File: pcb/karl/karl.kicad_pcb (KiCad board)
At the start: 2 copper layers, 72.4 x 57.1 mm, 30 parts, among them J1 Raspberry_Pi, J2 Power, J3 Battery, J4 LIDAR_Power, J5 Motor_Power, Q1 MMBT3904, Q2 MMBT3904, U1 MCP3421A0T-ECH

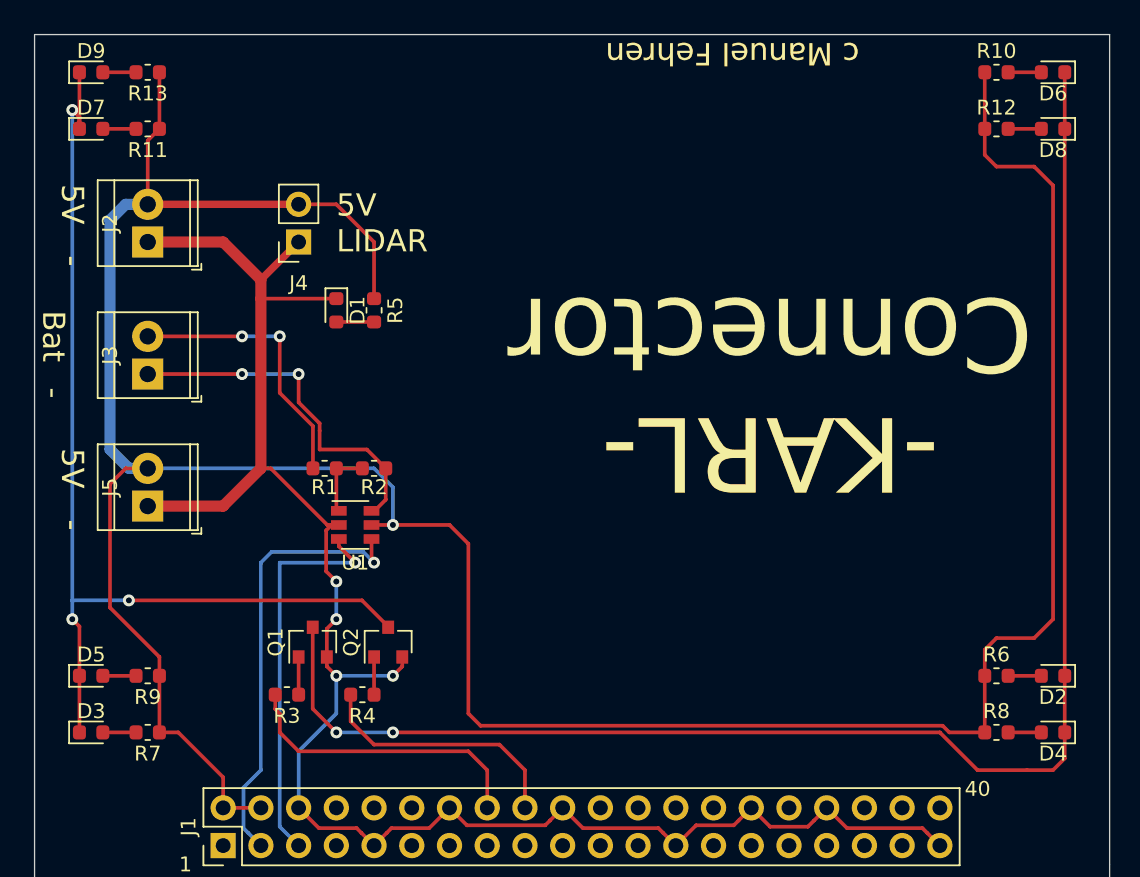
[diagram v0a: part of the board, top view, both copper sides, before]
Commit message: changes screw terminal
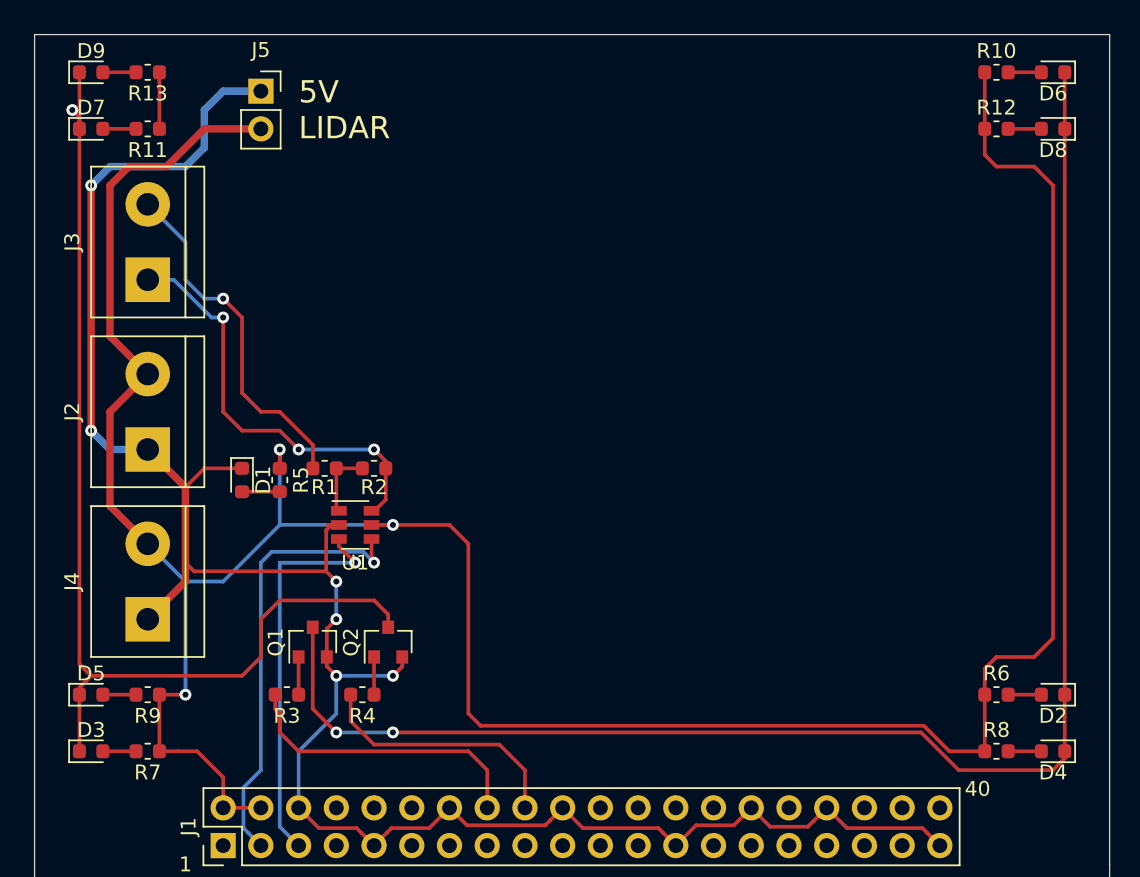
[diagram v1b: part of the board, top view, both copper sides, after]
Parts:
- J2, J3: footprint TerminalBlock_TE-Connectivity:TerminalBlock_TE_282834-2_1x02_P2.54mm_Horizontal -> TerminalBlock:TerminalBlock_bornier-2_P5.08mm
- J4: value LIDAR_Power -> Motor Power; footprint Connector_PinSocket_2.54mm:PinSocket_1x02_P2.54mm_Vertical -> TerminalBlock:TerminalBlock_bornier-2_P5.08mm
- J5: value Motor_Power -> LIDAR_Power; footprint TerminalBlock_TE-Connectivity:TerminalBlock_TE_282834-2_1x02_P2.54mm_Horizontal -> Connector_PinSocket_2.54mm:PinSocket_1x02_P2.54mm_Vertical
- moved J5 29.0 mm to (41.9, 24.1), turned to 0 degrees
- moved J4 27.4 mm to (34.3, 59.7), turned to 90 degrees
- moved J2 14.0 mm to (34.3, 48.3)
- moved D1 13.1 mm to (40.6, 50.3)
- moved R5 13.1 mm to (43.2, 50.3)
- moved J3 6.35 mm to (34.3, 36.8)
- moved D2 1.27 mm to (95.2, 64.8)
- moved D3 1.27 mm to (30.5, 68.6)
- moved D4 1.27 mm to (95.2, 68.6)
- moved D5 1.27 mm to (30.5, 64.8)
- moved R6 1.27 mm to (91.4, 64.8)
- moved R7 1.27 mm to (34.3, 68.6)
- moved R8 1.27 mm to (91.4, 68.6)
- moved R9 1.27 mm to (34.3, 64.8)
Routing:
- net GND: track 122.9 -> 142.1 mm, vias 4 -> 6
- net +5V: track 206.6 -> 197.9 mm, vias 1 -> 3
- net +BATT: track 18.7 -> 23.9 mm, vias 2 -> 1
- net GNDA: track 24.2 -> 28.7 mm, vias 2 -> 3
- net Net-(D3-Pad1): track 69.0 -> 72.3 mm, vias 3 -> 1
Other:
- board text removed: "-"
- board text removed: "-KARL-"
- board text removed: "-KARL- Connector"
- board text removed: "5V"
- board text removed: "Bat"
- board text removed: "c Manuel Fehren"

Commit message: added Pi Hat layout and OLED display
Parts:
- added H1: MountingHole, myFP:MountingHole_2.75mm_NoPad, F.Cu at (269.5, 128.4)
- added H2: MountingHole, myFP:MountingHole_2.75mm_NoPad, F.Cu at (211.5, 128.4)
- added H5: MountingHole, myFP:MountingHole_2.75mm_NoPad, F.Cu at (269.5, 79.4)
- added H6: MountingHole, myFP:MountingHole_2.75mm_NoPad, F.Cu at (211.5, 79.4)
- added J6: Motor A, TerminalBlock:TerminalBlock_bornier-2_P5.08mm, F.Cu at (259.1, 80.0)
- added J7: Motor B, TerminalBlock:TerminalBlock_bornier-2_P5.08mm, F.Cu at (247.7, 80.0)
- added U2: PCA9685PW, Package_SO:TSSOP-28_4.4x9.7mm_P0.65mm, F.Cu at (254.0, 92.7)
- added U3: DRV8848, Package_SO:TSSOP-16-1EP_4.4x5mm_P0.65mm, F.Cu at (243.8, 88.9)
- J3: footprint TerminalBlock:TerminalBlock_bornier-2_P5.08mm -> Connector_PinHeader_2.54mm:PinHeader_1x02_P2.54mm_Vertical
- J4: value Motor Power -> OLED; footprint TerminalBlock:TerminalBlock_bornier-2_P5.08mm -> Connector_PinHeader_2.54mm:PinHeader_1x04_P2.54mm_Vertical
- moved J2 243.6 mm to (270.5, 108.0)
- moved J3 237.8 mm to (259.1, 114.3)
- moved J5 235.9 mm to (262.9, 106.7), turned to 180 degrees
- moved J1 231.3 mm to (264.7, 127.1), turned to 270 degrees
- moved R2 223.6 mm to (262.2, 118.5)
- moved R1 223.6 mm to (258.9, 118.5)
- moved U1 223.6 mm to (260.9, 122.3)
- moved R3 211.0 mm to (246.4, 123.2), turned to 0 degrees
- moved Q1 209.7 mm to (246.7, 120.0)
- moved R4 202.0 mm to (242.1, 123.2), turned to 0 degrees
- moved Q2 200.6 mm to (242.2, 120.0)
- moved J4 196.6 mm to (228.6, 89.5)
- moved D1 193.5 mm to (219.6, 123.9), turned to 0 degrees
- moved D7 191.2 mm to (210.8, 90.2)
- moved D9 191.2 mm to (210.8, 86.4)
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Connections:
- J3 pad 1: GNDA -> +BATT
- J3 pad 2: +BATT -> GNDA
- J4 pad 2: +5V -> +3V3
- R3 pad 2: GPIO_23 -> PWM_04
- R4 pad 2: GPIO_24 -> PWM_05
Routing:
- net +3V3: track 0.00 -> 130.5 mm, vias 0 -> 1
- net PWM_05: track 0.00 -> 72.5 mm, vias 0 -> 2
- net SCL: track 26.7 -> 94.1 mm, vias 1 -> 2
- net PWM_04: track 0.00 -> 66.5 mm, vias 0 -> 2
- net SDA: track 29.9 -> 91.6 mm, vias 1 -> 3
- net GND: track 142.1 -> 202.4 mm, vias 6 -> 2
- net +5V: track 197.9 -> 156.1 mm
- net Net-(D2-Pad1): track 104.4 -> 69.0 mm
- net GPIO_23: track 20.2 -> 0.00 mm
- net GNDA: track 28.7 -> 10.4 mm, vias 3 -> 1
- net GPIO_24: track 17.4 -> 0.00 mm
- net Net-(J6-Pad1): track 0.00 -> 16.7 mm
- net +BATT: track 23.9 -> 8.09 mm
- net PWM_02: track 0.00 -> 13.6 mm
- net Net-(J6-Pad2): track 0.00 -> 12.9 mm
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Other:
- board size 72.4 x 57.1 mm -> 67 x 56.6 mm
- board text removed: "1"
- board text removed: "5V LIDAR"

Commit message: added MPU6050
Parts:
- added C1: 10nF, Capacitor_SMD:C_0201_0603Metric, F.Cu at (144.3, 94.7)
- added C2: 0.1µF, Capacitor_SMD:C_0201_0603Metric, F.Cu at (148.1, 89.8)
- added C3: 2.2nF, Capacitor_SMD:C_0201_0603Metric, F.Cu at (148.1, 88.1)
- added C4: 0.1µF, Capacitor_SMD:C_0201_0603Metric, F.Cu at (145.5, 94.7)
- added U4: MPU-6050, Sensor_Motion:InvenSense_QFN-24_4x4mm_P0.5mm, F.Cu at (145.0, 90.7)
- moved D6 91.8 mm to (181.0, 78.7)
- moved D8 91.8 mm to (181.0, 81.3)
- moved R10 91.8 mm to (177.2, 78.7)
- moved R12 91.8 mm to (177.2, 81.3)
- moved R2 91.8 mm to (170.8, 110.8)
- moved D1 91.8 mm to (128.1, 116.2)
- moved D2 91.8 mm to (181.1, 111.8)
- moved D3 91.8 mm to (119.4, 114.3)
- moved D4 91.8 mm to (181.1, 114.4)
- moved D5 91.8 mm to (119.4, 111.8)
- moved D7 91.8 mm to (119.4, 82.5)
- moved D9 91.8 mm to (119.4, 78.7)
- moved H1 91.8 mm to (178.1, 120.8)
- moved H2 91.8 mm to (120.1, 120.8)
- moved H5 91.8 mm to (178.1, 71.8)
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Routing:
- net +5V: track 156.1 -> 263.5 mm, vias 3 -> 4
- net GND: track 202.4 -> 222.5 mm, vias 2 -> 4
- net SDA: track 91.6 -> 97.8 mm, vias 3 -> 4
- net SCL: track 94.1 -> 99.1 mm, vias 2 -> 4
- net Net-(C3-Pad2): track 0.00 -> 3.21 mm
- net Net-(C4-Pad2): track 0.00 -> 1.92 mm
- net Net-(C1-Pad2): track 0.00 -> 1.81 mm

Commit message: minor changes
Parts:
- moved J5 3.56 mm to (167.9, 99.1)
- moved J2 0.25 mm to (178.8, 100.3)
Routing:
- net GND: track 222.5 -> 226.0 mm
- net +5V: track 263.5 -> 267.0 mm
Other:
- board text added: "+"
- board text added: "-"
- board text added: "5V"
- board text added: "KARL Pi-HAT"
- board text added: "M-A"
- board text added: "M-B"
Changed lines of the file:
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@@
   (general
     (thickness 1.6)
-    (drawings 13)
-    (tracks 463)
+    (drawings 19)
+    (tracks 465)
     (zones 0)
     (modules 43)
@@
   )
   (setup
-    (last_trace_width 0.25)
+    (last_trace_width 1)
     (user_trace_width 0.4)
     (user_trace_width 0.5)
@@
   )
   (module Connector_PinSocket_2.54mm:PinSocket_1x02_P2.54mm_Vertical (layer F.Cu)
-    (at 171.45 99.06 180)
+    (at 167.894 99.06 180)
     (descr "Through hole straight socket strip, 1x02, 2.54mm pitch, single row (from Kicad 4.0.7), script generated")
     (tags "Through hole socket strip THT 1x02 2.54mm single row")
@@
   )
   (module TerminalBlock:TerminalBlock_bornier-2_P5.08mm (layer F.Cu)
-    (at 179.07 100.33 90)
+    (at 178.816 100.33 90)
     (descr "simple 2-pin terminal block, pitch 5.08mm, revamped version of bornier2")
     (tags "terminal block bornier2")
-    (fp_text reference J2 (at 2.54 -5.08 90) (layer F.SilkS)
+    (fp_text reference J2 (at 2.54 -5.08 90) (layer F.SilkS) hide
       (effects (font (size 1 1) (thickness 0.15)))
     )
@@
   (module myFP:MountingHole_2.75mm_NoPad (layer F.Cu)
     (at 178.06 120.78 180)
-    (fp_text reference H1 (at 0 3.5) (layer F.SilkS)
+    (fp_text reference H1 (at 0 3.5) (layer F.SilkS) hide
       (effects (font (size 1 1) (thickness 0.15)))
     )
@@
       (effects (font (size 1 1) (thickness 0.15)))
     )
-    (fp_text user %R (at 0 0) (layer F.Fab)
+    (fp_text user %R (at 0 0 90) (layer F.Fab)
       (effects (font (size 1 1) (thickness 0.15)))
     )
@@
   (module myFP:MountingHole_2.75mm_NoPad (layer F.Cu)
     (at 120.06 120.78 180)
-    (fp_text reference H2 (at 0.426 2.162) (layer F.SilkS)
+    (fp_text reference H2 (at 0.426 2.162) (layer F.SilkS) hide
       (effects (font (size 1 1) (thickness 0.15)))
     )
@@
   (module myFP:MountingHole_2.75mm_NoPad (layer F.Cu)
     (at 120.06 71.78 180)
-    (fp_text reference H6 (at -0.59 1.168) (layer F.SilkS)
+    (fp_text reference H6 (at -0.59 1.168) (layer F.SilkS) hide
       (effects (font (size 1 1) (thickness 0.15)))
     )
@@
   (module myFP:MountingHole_2.75mm_NoPad (layer F.Cu)
     (at 178.06 71.78 180)
-    (fp_text reference H5 (at 0.006 -0.102) (layer F.SilkS)
+    (fp_text reference H5 (at 0.006 -0.102) (layer F.SilkS) hide
       (effects (font (size 1 1) (thickness 0.15)))
     )
@@
     (pad "" np_thru_hole circle (at 0 0 180) (size 2.75 2.75) (drill 2.75) (layers *.Cu *.Mask)
       (solder_mask_margin 1.375))
+  )
+  (gr_text - (at 178.816 104.902 90) (layer F.SilkS)
+    (effects (font (size 3 3) (thickness 0.3)))
+  )
+  (gr_text + (at 178.816 90.678 90) (layer F.SilkS)
+    (effects (font (size 3 3) (thickness 0.3)))
+  )
+  (gr_text 5V (at 172.72 97.79 90) (layer F.SilkS)
+    (effects (font (size 3 3) (thickness 0.3)))
+  )
+  (gr_text M-A (at 172.72 75.692) (layer F.SilkS)
+    (effects (font (size 1.5 1.5) (thickness 0.3)))
+  )
+  (gr_text "M-B\n" (at 145.796 75.438) (layer F.SilkS)
+    (effects (font (size 1.5 1.5) (thickness 0.3)))
+  )
+  (gr_text "KARL Pi-HAT" (at 134.366 71.882) (layer F.SilkS)
+    (effects (font (size 2 2) (thickness 0.4)))
   )
   (gr_line (start 154.94 79.375) (end 154.94 106.68) (layer F.SilkS) (width 0.3))
@@
   (segment (start 149.062151 87.863097) (end 149.062151 83.162849) (width 0.25) (layer B.Cu) (net 2))
   (segment (start 149.062151 83.162849) (end 149.445 82.78) (width 0.25) (layer B.Cu) (net 2))
+  (segment (start 171.45 99.06) (end 167.894 99.06) (width 1) (layer F.Cu) (net 2))
   (segment (start 139.7 81.915) (end 142.875 85.09) (width 0.25) (layer F.Cu) (net 19))
   (segment (start 142.875 85.09) (end 143.51 85.725) (width 0.25) (layer F.Cu) (net 19))
@@
   (segment (start 150.368 86.36) (end 153.27 86.36) (width 0.25) (layer B.Cu) (net 28))
   (segment (start 149.787152 86.940848) (end 150.368 86.36) (width 0.25) (layer B.Cu) (net 28))
+  (segment (start 171.45 96.52) (end 167.894 96.52) (width 1) (layer F.Cu) (net 28))
   (segment (start 170.61 119.37) (end 170.72 119.48) (width 0.25) (layer F.Cu) (net 29))
   (segment (start 170.61 115.61) (end 170.61 119.37) (width 0.25) (layer F.Cu) (net 29))
